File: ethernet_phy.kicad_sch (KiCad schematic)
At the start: 24 parts, among them U1 RTL8201F

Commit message: Use kicad symbol for the optotransistor
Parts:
- RJ1: footprint project specific:RJ45-TH_HY931147C -> project_footprints:RJ45-TH_HY931147C
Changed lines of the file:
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@@
 			)
 		)
-		(property "Footprint" "project specific:RJ45-TH_HY931147C"
+		(property "Footprint" "project_footprints:RJ45-TH_HY931147C"
 			(at 279.4 124.46 0)
 			(effects

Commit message: Finish routing
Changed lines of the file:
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@@
+	)
+	(junction
+		(at 243.84 104.14)
+		(diameter 0)
+		(color 0 0 0 0)
 	)
 	(junction
@@
 		(pts
 			(xy 83.185 69.85) (xy 87.63 69.85)
-		)
-		(stroke
-			(width 0)
-			(type default)
-		)
-	)
-	(wire
-		(pts
-			(xy 243.84 104.775) (xy 246.38 104.775)
 		)
 		(stroke
@@
 		(lib_name "GND_1")
 		(lib_id "power:GND")
-		(at 246.38 104.775 270)
+		(at 243.84 104.14 270)
 		(mirror x)
 		(unit 1)
@@
 		(fields_autoplaced yes)
 		(property "Reference" "#PWR0110"
-			(at 240.03 104.775 0)
+			(at 237.49 104.14 0)
 			(effects
 				(font
@@
 		)
 		(property "Value" "GND"
-			(at 243.205 104.7749 90)
+			(at 240.665 104.1399 90)
 			(effects
 				(font
@@
 		)
 		(property "Footprint" ""
-			(at 246.38 104.775 0)
+			(at 243.84 104.14 0)
 			(effects
 				(font
@@
 		)
 		(property "Datasheet" ""
-			(at 246.38 104.775 0)
+			(at 243.84 104.14 0)
 			(effects
 				(font
@@
 		)
 		(property "Description" ""
-			(at 246.38 104.775 0)
-			(effects
-				(font
+			(at 243.84 104.14 0)
+			(effects
+				(font

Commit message: BOM updates
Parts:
- RJ1: LCSC (none) -> C91754
- TP5: now left out of the parts list
- U1: LCSC (none) -> C45044

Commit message: Zamkonator rev 1.3
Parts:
- renumbered C9 to C10, C5 to C11, C3 to C12, C1 to C3, C2 to C4, C10 to C5, C4 to C6, C6 to C7, C7 to C8, C8 to C9, D1 to D6, R8 to R10, R6 to R11, R5 to R12, R4 to R13, R3 to R14, R1 to R15, R2 to R16, R7 to R8, TP5 to TP16, U1 to U2

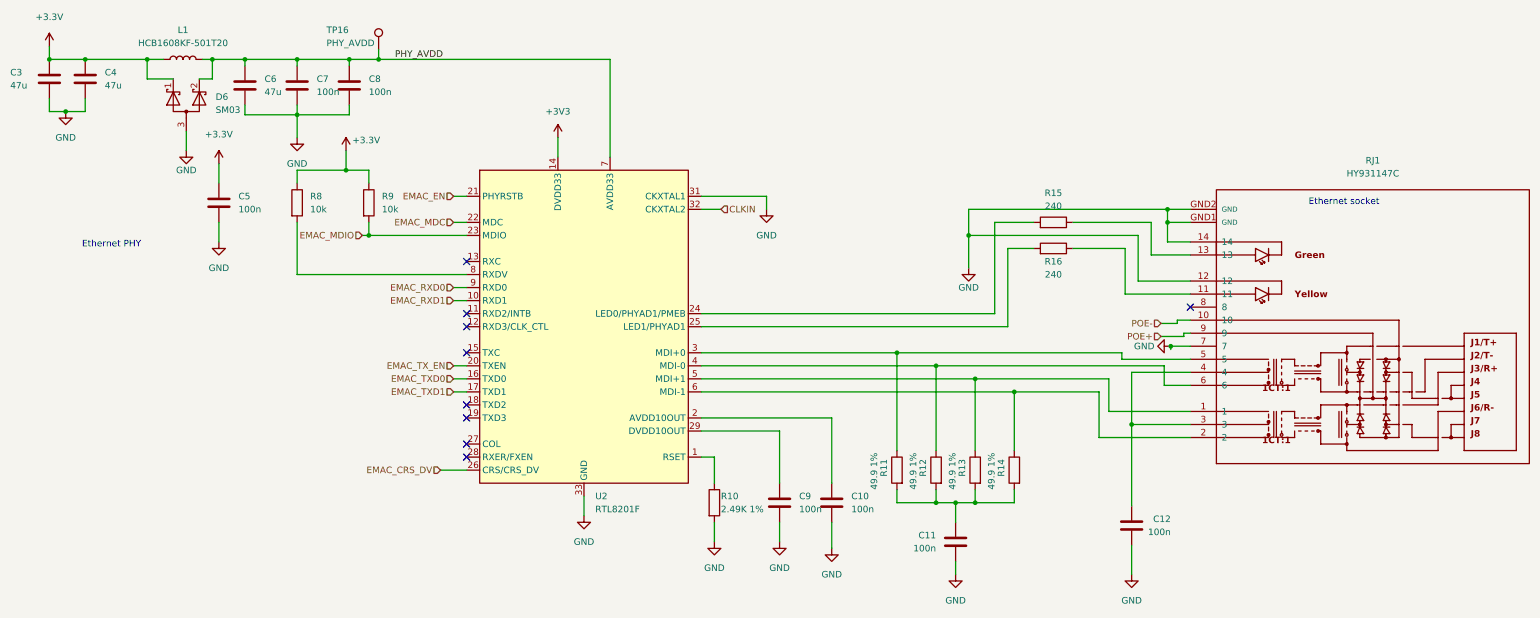
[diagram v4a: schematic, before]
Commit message: Rev 1.3, BOM optimizations
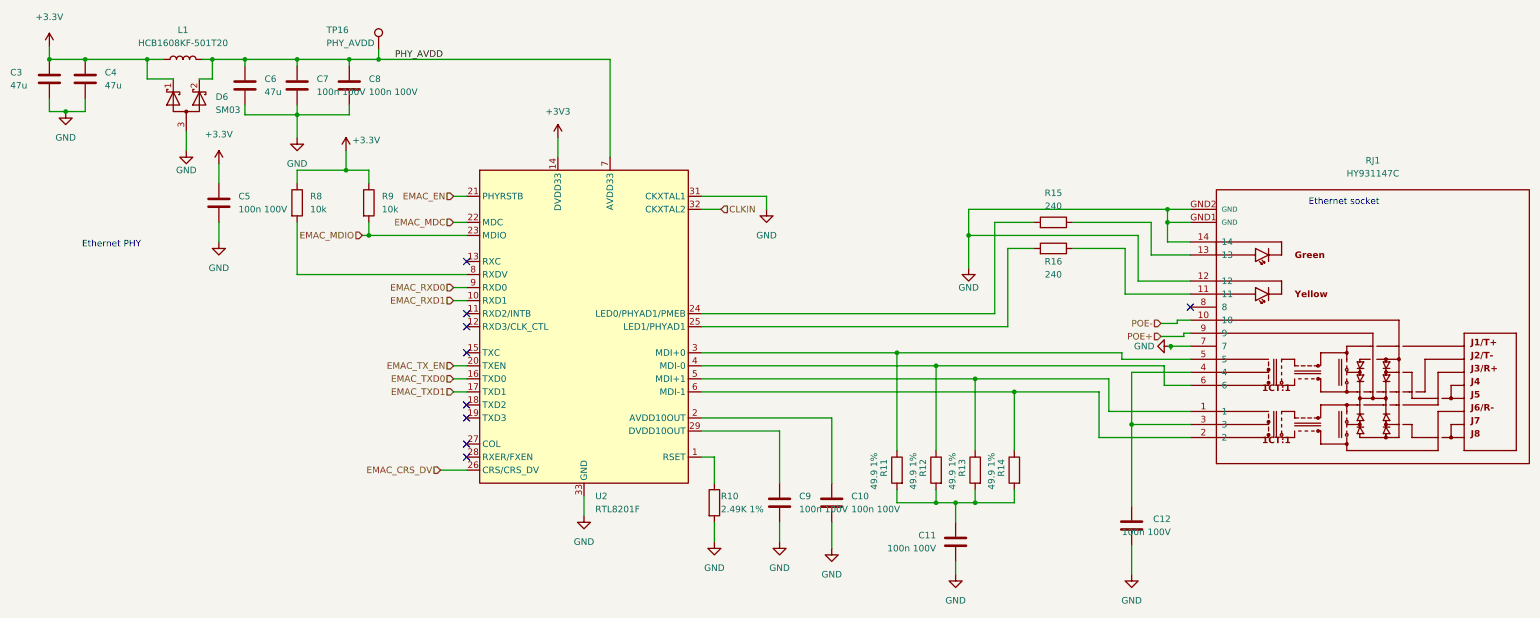
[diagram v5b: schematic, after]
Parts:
- C10, C11, C12, C5, C7, C8, C9: value 100n -> 100n 100V
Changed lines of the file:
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@@
 			)
 		)
-		(property "Value" "100n"
+		(property "Value" "100n 100V"
 			(at 77.47 54.6099 0)
 			(show_name no)
@@
 			)
 		)
-		(property "Value" "100n"
+		(property "Value" "100n 100V"
 			(at 198.12 143.5099 0)
 			(show_name no)
@@
 			)
 		)
-		(property "Value" "100n"
+		(property "Value" "100n 100V"
 			(at 62.23 77.4699 0)
 			(show_name no)
@@
 			)
 		)
-		(property "Value" "100n"
+		(property "Value" "100n 100V"
 			(at 87.63 54.6099 0)
 			(show_name no)
@@
 			)
 		)
-		(property "Value" "100n"
+		(property "Value" "100n 100V"
 			(at 181.61 135.8899 0)
 			(show_name no)
@@
 			)
 		)
-		(property "Value" "100n"
+		(property "Value" "100n 100V"
 			(at 243.84 140.335 0)
 			(show_name no)
@@
 			)
 		)
-		(property "Value" "100n"
+		(property "Value" "100n 100V"
 			(at 171.45 135.8899 0)
 			(show_name no)
